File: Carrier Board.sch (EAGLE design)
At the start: 56 parts, among them J4 S2B-PH-SM4-TB(LF)(SN), J5 S2B-PH-SM4-TB(LF)(SN), Q1 MMBT2222A, U1 TMP36GRTZ, U2 TPL5010, U3 MB85RC256, U4 Particle Electron, U5 TPS22810, U6 TPS22810, U7 NAND

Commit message: v0.1 - First rough layout
Just getting started.
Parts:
- removed C6, C7: 0.1uF, SparkFun-Capacitors:CAP0805
- removed J1, J2/SPI: (no value), SparkFun-Connectors:CONN_03X22X3_SILK_MALE_PTH
- removed R8, R9: 100, SparkFun-Passives:RESISTOR0805-RES
- removed U4: Particle Electron, Particle-Devices:ELECTRON-PWR-PINS
- removed U5, U6: TPS22810, Custom Components:TPS22810
- added BORON: PARTICLE-DEVICES-BORON, Carrier Board:PARTICLE-DEVICES-BORON
- added JP8: (no value), SparkFun-Connectors:M06LOCK
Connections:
- removed net A4: J2/SPI.3, U4.A4
- removed net B0: U4.B0
- removed net B1: J1.1, U4.B1
- removed net B2: J1.3, U4.B2
- removed net B3: J1.5, U4.B3
- removed net B4: J1.4, U4.B4
- removed net BATT-IN: D2.ANODE, J5.+, U6.VIN
- removed net C0: U4.C0
- removed net C1: U4.C1
- removed net C2: JP2.2, U4.C2
- removed net C3: JP2.3, U4.C3
- removed net C4: JP2.4, U4.C4
- removed net C5: JP2.5, U4.C5
- removed net DAC: U4.DAC
- removed net DC-IN: C8.P$1, D3.ANODE, F1.2, U5.VIN, V1.2
- removed net N$2: C6.1, U5.CT
- removed net N$5: C7.1, U6.CT
- removed net N$6: R8.1, U6.QOD
- removed net N$7: R9.1, U5.QOD
- removed net ON/OFF: U5.EN/UVLO, U6.EN/UVLO, U7A.O
- removed net VIN: R9.2, U4.VIN, U5.VOUT
- new net 3V3: BORON.3V3
- new net A0: BORON.A0, JP8.5
- new net D7: BORON.D7
- new net EN: BORON.EN, U7A.O
- new net MD: BORON.MD
- new net MISO: BORON.MI, JP2.3
- new net MOSI: BORON.MO, JP2.4
- new net SCK: BORON.SCK, JP2.5
- new net VUSB: BORON.VUSB, C8.P$1, D3.ANODE, F1.2, V1.2
- new net WAKE: BORON.D6
- net !RST: now also BORON.!RST; no longer U4.!RST
- net !SHTDWN: now also BORON.D8; no longer U4.B5
- net A1: now also BORON.A1, JP8.4; no longer U4.A1
- net A2: now also BORON.A2, JP8.3; no longer J2/SPI.4, U4.A2
- net A3: now also BORON.A3, JP8.2; no longer J2/SPI.1, U4.A3
- net A5: now also BORON.A5, JP2.2; no longer J2/SPI.5, U4.A5
- net D2: now also BORON.D2; no longer U4.D2
- net D3: now also BORON.D3; no longer U4.D3
- net DONE: now also BORON.D5; no longer U4.D6
- net GND: now also BORON.GND, JP8.1; no longer C6.2, C7.2, J1.6, J2/SPI.6, U4.GND@2, U4.GND@21, U5.GND, U6.GND
- net HARD-RESET: no longer U4.D4
- net LI+: now also BORON.LI+, D2.ANODE, J5.+; no longer R8.2, U4.LI+, U6.VOUT
- net RX: now also BORON.RX; no longer U4.RX
- net SCL: now also BORON.SCL; no longer U4.D1
- net SDA: now also BORON.SDA; no longer U4.D0
- net TEMP: now also BORON.A4; no longer U4.A0
- net TX: now also BORON.TX; no longer U4.TX
- net USER-SW: now also BORON.D4; no longer U4.D5
- net VCC: now also JP8.6; no longer J1.2, J2/SPI.2, JP2.6, U4.3V3
- net VCC-EXT: now also JP2.6
- net WKP: no longer U4.WKP

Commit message: v0.11 - Refining placments
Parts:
- removed S1: B3F-1070, switch-omron:10-XX
- added SW2: MF-SW-TACT-6MM, MF_Switches:TACT_6MM
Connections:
- removed net WKP: U2.WAKE
- net GND: now also SW2.P$3, SW2.P$4; no longer S1.P, S1.P1
- net N$4: now also SW2.P$1, SW2.P$2; no longer S1.S, S1.S1
- net WAKE: now also U2.WAKE

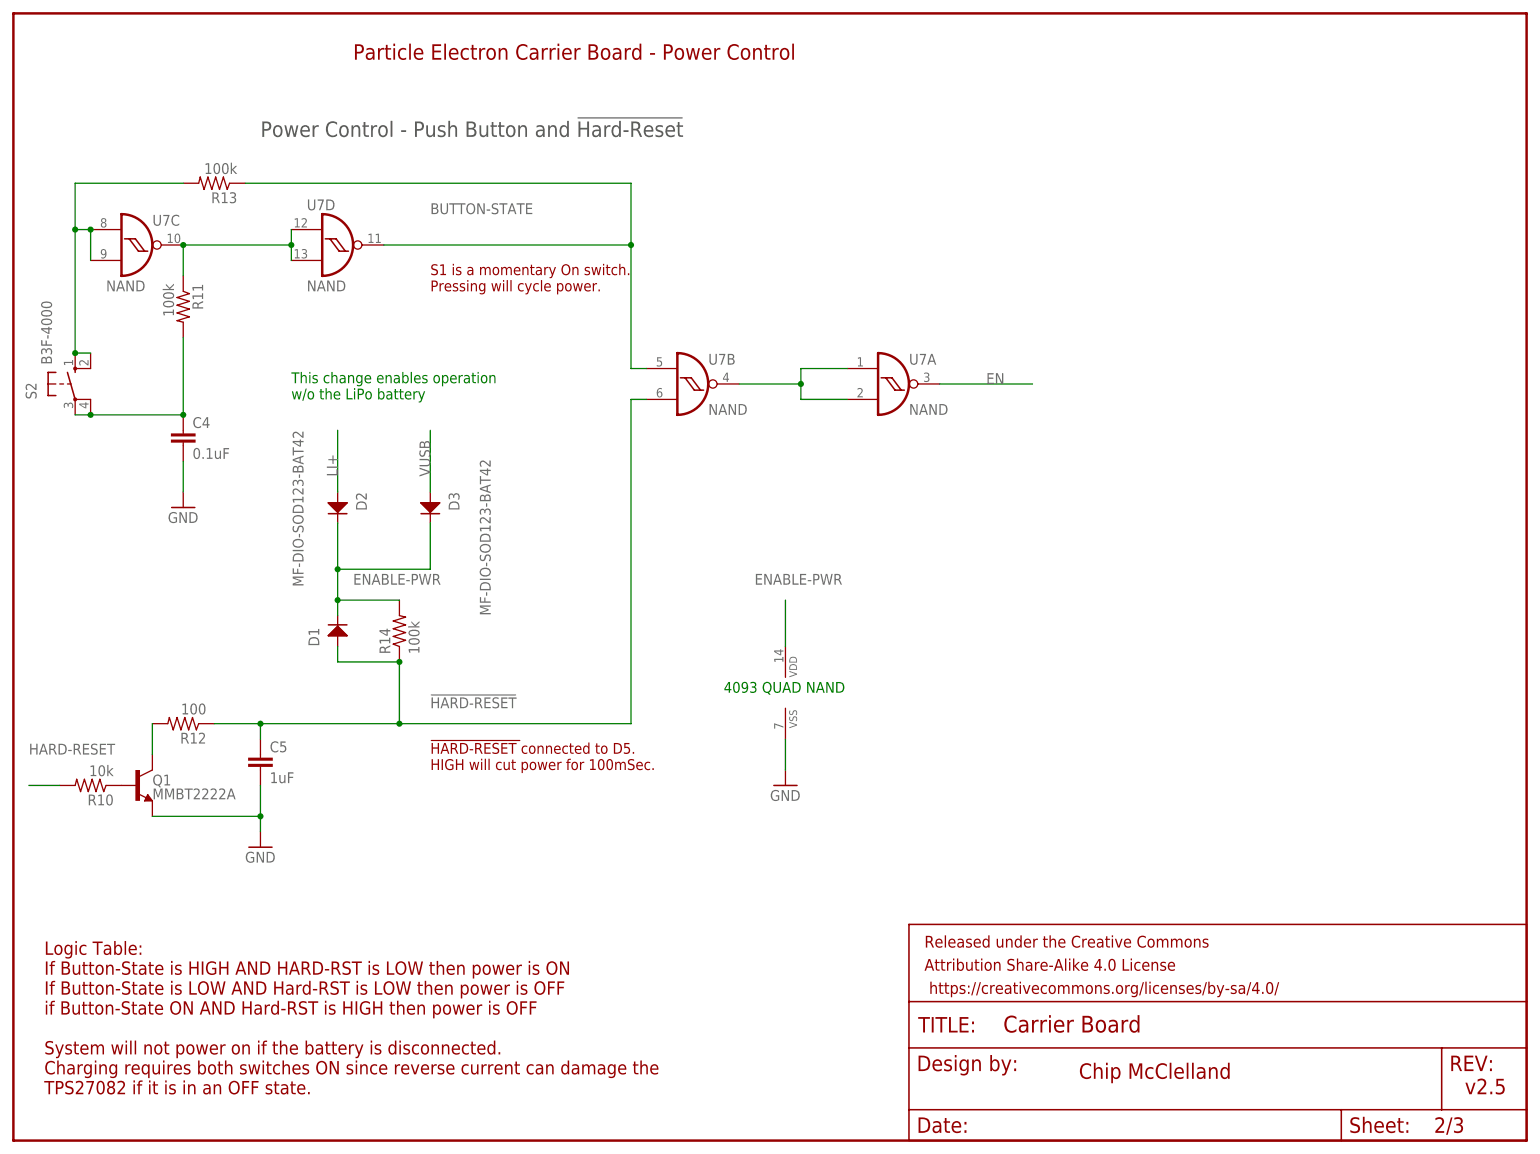
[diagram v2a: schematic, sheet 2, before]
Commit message: More tweaks
D8 for wake, no shutdown on TMP-36 and Hard-reset connected.  Power protection for off-board VCC
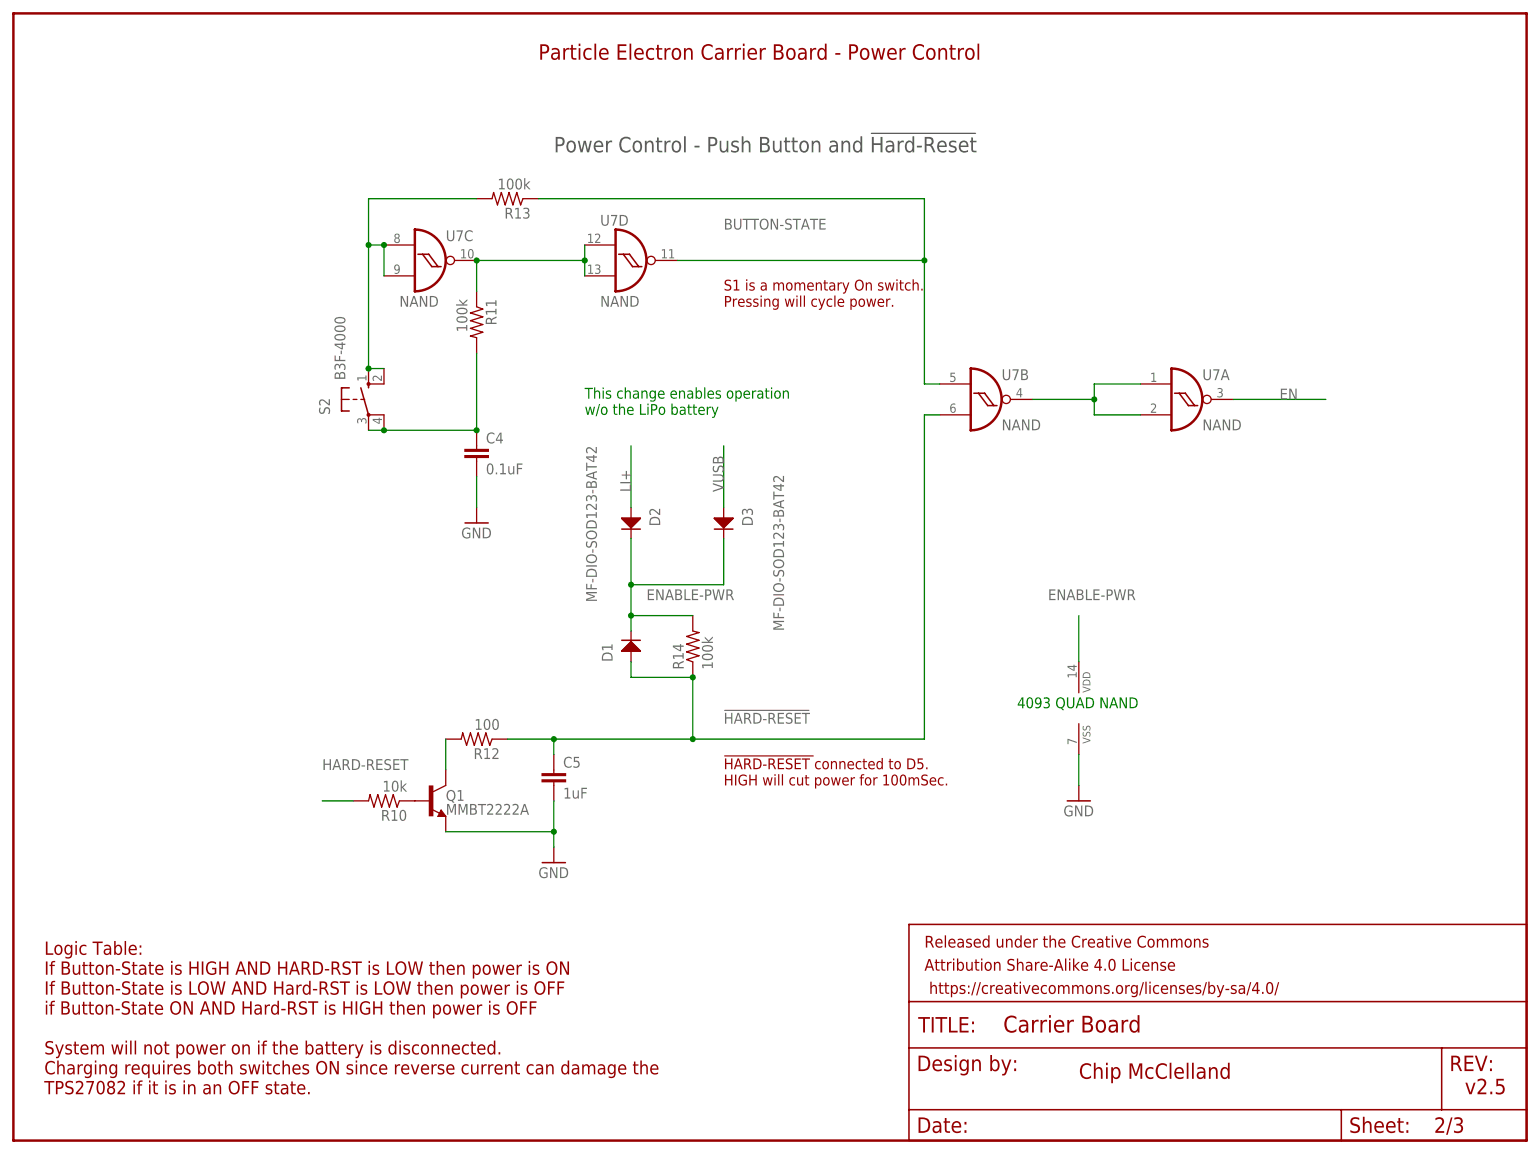
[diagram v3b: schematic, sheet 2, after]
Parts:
- added F2: 500mA - FAST BLOW, SparkFun-Fuses:PPTC_HALF-AMP
- added V2: VC080505C150DP, Custom Components:VARISTOR
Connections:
- net A5 renamed SS
- removed net !SHTDWN: BORON.D8, U1.!SHTDWN
- new net VCC2-EXT: F2.2, JP1.6, V2.2
- net GND: now also JP8.6, V2.1; no longer JP8.1
- net HARD-RESET: now also BORON.D6
- net VCC: now also F2.1, U1.!SHTDWN; no longer JP8.6
- net VCC-EXT: now also JP8.1; no longer JP1.6
- net WAKE: now also BORON.D8; no longer BORON.D6
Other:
- note added: "Ran out of pins so will not implement !Shutdown on the TMP-36. It draws only about 50uA"
- moved on the sheet: C4, C5, C8, D1, D2, D3, F1, F3, G1, J3, J4, J5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

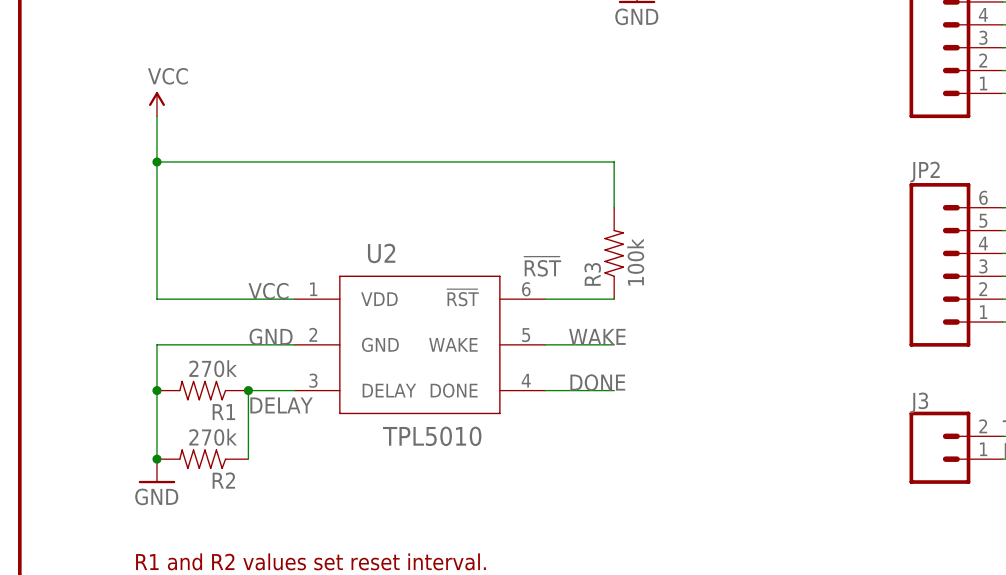
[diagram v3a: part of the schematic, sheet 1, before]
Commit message: Added Heratch's v3 starter
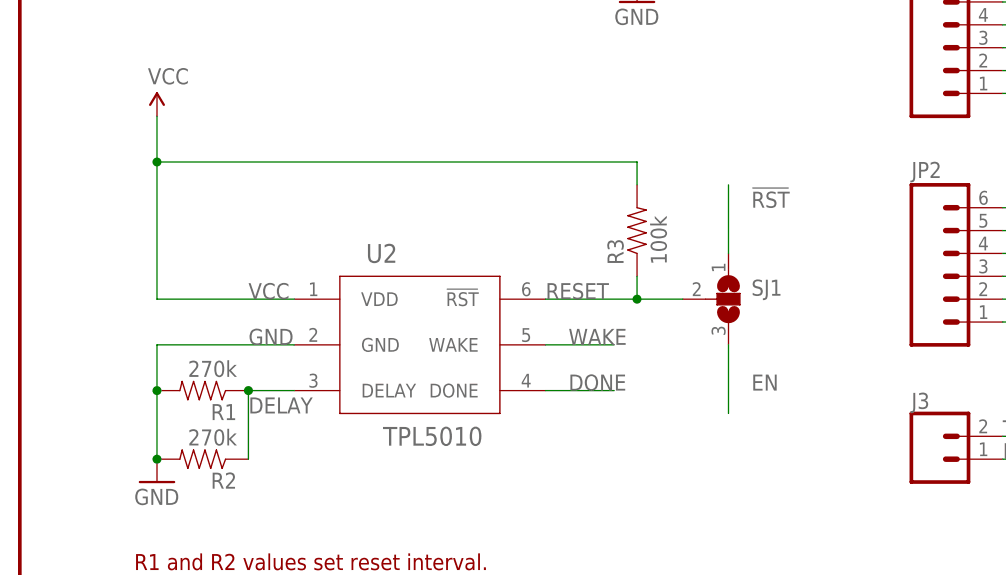
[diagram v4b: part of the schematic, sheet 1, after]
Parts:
- added SJ1: (no value), jumper:SJ2W
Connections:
- new net RESET: R3.1, SJ1.2, U2.!RST
- net !RST: now also SJ1.1; no longer R3.1, U2.!RST
- net EN: now also SJ1.3
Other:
- moved on the sheet: R3
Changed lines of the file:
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@@
 <part name="V2" library="Custom Components" deviceset="VARISTOR" device="" value="VC080505C150DP "/>
 <part name="F2" library="SparkFun-Fuses" deviceset="PPTC" device="_HALF-AMP" value="500mA - FAST BLOW"/>
+<part name="SJ1" library="jumper" library_urn="urn:adsk.eagle:library:252" deviceset="SJ2W" device="" package3d_urn="urn:adsk.eagle:package:15474/1"/>
 </parts>
 <sheets>
@@
 <attribute name="NAME" x="99.06" y="86.868" size="1.778" layer="95" font="vector"/>
 </instance>
-<instance part="R3" gate="G$1" x="66.04" y="104.14" smashed="yes" rot="R90">
-<attribute name="NAME" x="64.5414" y="100.33" size="1.778" layer="95" rot="R90"/>
-<attribute name="VALUE" x="69.342" y="100.33" size="1.778" layer="96" rot="R90"/>
+<instance part="R3" gate="G$1" x="68.58" y="106.68" smashed="yes" rot="R90">
+<attribute name="NAME" x="67.0814" y="102.87" size="1.778" layer="95" rot="R90"/>
+<attribute name="VALUE" x="71.882" y="102.87" size="1.778" layer="96" rot="R90"/>
 </instance>
 <instance part="R4" gate="G$1" x="96.52" y="38.1" smashed="yes" rot="R90">
@@
 <attribute name="NAME" x="91.44" y="30.48" size="1.016" layer="95" font="vector" align="top-left"/>
 <attribute name="VALUE" x="91.44" y="27.94" size="1.016" layer="96" font="vector"/>
+</instance>
+<instance part="SJ1" gate="G$1" x="78.74" y="99.06" smashed="yes">
+<attribute name="NAME" x="81.28" y="99.441" size="1.778" layer="95"/>
+<attribute name="VALUE" x="81.28" y="97.155" size="1.778" layer="96"/>
 </instance>
 </instances>
@@
 <pinref part="SUPPLY2" gate="G$1" pin="VCC"/>
 <pinref part="R3" gate="G$1" pin="2"/>
-<wire x1="15.24" y1="114.3" x2="66.04" y2="114.3" width="0.1524" layer="91"/>
-<wire x1="66.04" y1="114.3" x2="66.04" y2="109.22" width="0.1524" layer="91"/>
+<wire x1="15.24" y1="114.3" x2="68.58" y2="114.3" width="0.1524" layer="91"/>
 <wire x1="15.24" y1="114.3" x2="15.24" y2="119.38" width="0.1524" layer="91"/>
 <wire x1="15.24" y1="99.06" x2="30.48" y2="99.06" width="0.1524" layer="91"/>
@@
 <pinref part="U2" gate="G$1" pin="VDD"/>
 <label x="25.4" y="99.06" size="1.778" layer="95"/>
+<wire x1="68.58" y1="114.3" x2="68.58" y2="111.76" width="0.1524" layer="91"/>
 </segment>
 <segment>
@@
 <net name="!RST" class="0">
 <segment>
-<wire x1="66.04" y1="99.06" x2="58.42" y2="99.06" width="0.1524" layer="91"/>
-<pinref part="R3" gate="G$1" pin="1"/>
-<pinref part="U2" gate="G$1" pin="!RST"/>
-<label x="55.88" y="101.6" size="1.778" layer="95"/>
-</segment>
-<segment>
 <pinref part="BORON" gate="G$1" pin="!RST"/>
 <wire x1="157.48" y1="167.64" x2="147.32" y2="167.64" width="0.1524" layer="91"/>
 <label x="149.86" y="167.64" size="1.778" layer="95"/>
+</segment>
+<segment>
+<pinref part="SJ1" gate="G$1" pin="1"/>
+<wire x1="78.74" y1="104.14" x2="78.74" y2="111.76" width="0.1524" layer="91"/>
+<label x="81.28" y="109.22" size="1.778" layer="95"/>
 </segment>
 </net>
@@
 <label x="198.12" y="142.24" size="1.778" layer="95" align="bottom-right"/>
 </segment>
+<segment>
+<pinref part="SJ1" gate="G$1" pin="3"/>
+<wire x1="78.74" y1="93.98" x2="78.74" y2="86.36" width="0.1524" layer="91"/>
+<label x="81.28" y="88.9" size="1.778" layer="95"/>
+</segment>
 </net>
 <net name="VUSB" class="0">
@@
 <wire x1="109.22" y1="134.62" x2="116.84" y2="134.62" width="0.1524" layer="91"/>
 <label x="111.76" y="134.62" size="1.778" layer="95"/>
+</segment>
+</net>
+<net name="RESET" class="0">
+<segment>
+<pinref part="R3" gate="G$1" pin="1"/>
+<pinref part="U2" gate="G$1" pin="!RST"/>
+<label x="58.42" y="99.06" size="1.778" layer="95"/>
+<pinref part="SJ1" gate="G$1" pin="2"/>
+<wire x1="58.42" y1="99.06" x2="68.58" y2="99.06" width="0.1524" layer="91"/>
+<wire x1="68.58" y1="99.06" x2="73.66" y2="99.06" width="0.1524" layer="91"/>
+<wire x1="68.58" y1="101.6" x2="68.58" y2="99.06" width="0.1524" layer="91"/>
+<junction x="68.58" y="99.06"/>
 </segment>
 </net>
@@
 with this version.
 </note>
+<note version="8.3" severity="warning">
+Since Version 8.3, EAGLE supports URNs for individual library
+assets (packages, symbols, and devices). The URNs of those assets
+will not be understood (or retained) with this version.
+</note>
+<note version="8.3" severity="warning">
+Since Version 8.3, EAGLE supports the association of 3D packages
+with devices in libraries, schematics, and board files. Those 3D
+packages will not be understood (or retained) with this version.
+</note>
 <note version="9.0" severity="warning">

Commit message: First Pass - Ready to send to OSHPark
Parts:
- removed SJ1: (no value), jumper:SJ2W
- added JP7: JUMPER-SMT_3_1-NC_TRACE_SILK, SparkFun-Jumpers:JUMPER-SMT_3_1-NC_TRACE_SILK
- added JP9: JUMPER-SMT_2_NC_PASTE_SILK, SparkFun-Jumpers:JUMPER-SMT_2_NC_PASTE_SILK
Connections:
- removed net 3V3: BORON.3V3
- removed net D7: BORON.D7
- new net VDD: JP9.1, U2.VDD
- net !RST: now also JP7.3; no longer SJ1.1
- net EN: now also JP7.1; no longer SJ1.3
- net RESET: now also JP7.2; no longer SJ1.2
- net VCC: now also BORON.3V3, JP9.2; no longer U2.VDD
